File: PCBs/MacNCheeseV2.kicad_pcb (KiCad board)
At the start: 2 copper layers, 102.4 x 81 mm, 33 parts, among them SW1 SW_Push, SW10 SW_Push, SW11 SW_Push, SW12 SW_Push, SW13 SW_Push, SW14 SW_Push, SW15 SW_Push, SW16 SW_Push, SW2 SW_Push, SW3 SW_Push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

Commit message: PCBs V2.1
Added Designs
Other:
- board text added: "7763"
- board text added: "Emily is Awesome!!"
- board text added: "What a Super Idea"
- board text removed: "Why?"
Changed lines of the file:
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@@
 		)
 		(fp_text user "K"
-			(at 0 -2.1 90)
+			(at 0 0 90)
 			(layer "F.SilkS")
 			(effects
@@
 		)
 		(fp_text user "K"
-			(at 0 -2.1 90)
+			(at 0 0 90)
 			(layer "F.Fab")
 			(effects
@@
 		)
 	)
+	(gr_text "7763"
+		(at 136.75 32.75 0)
+		(layer "F.SilkS")
+		(effects
+			(font
+				(size 1 1)
+				(thickness 0.1)
+			)
+			(justify left bottom)
+		)
+	)
 	(gr_text "XIAO HERE"
 		(at 144.5 50.25 0)
@@
 		)
 	)
+	(gr_text "Emily is Awesome!!"
+		(at 62.75 65.25 270)
+		(layer "F.SilkS")
+		(effects
+			(font
+				(size 1 1)
+				(thickness 0.1)
+			)
+			(justify left bottom)
+		)
+	)
 	(gr_text "YOTC"
 		(at 64 111.5 0)
@@
 		)
 	)
-	(gr_text "Why?"
+	(gr_text "What a Super Idea"
 		(at 64 32.75 0)
 		(layer "F.SilkS")

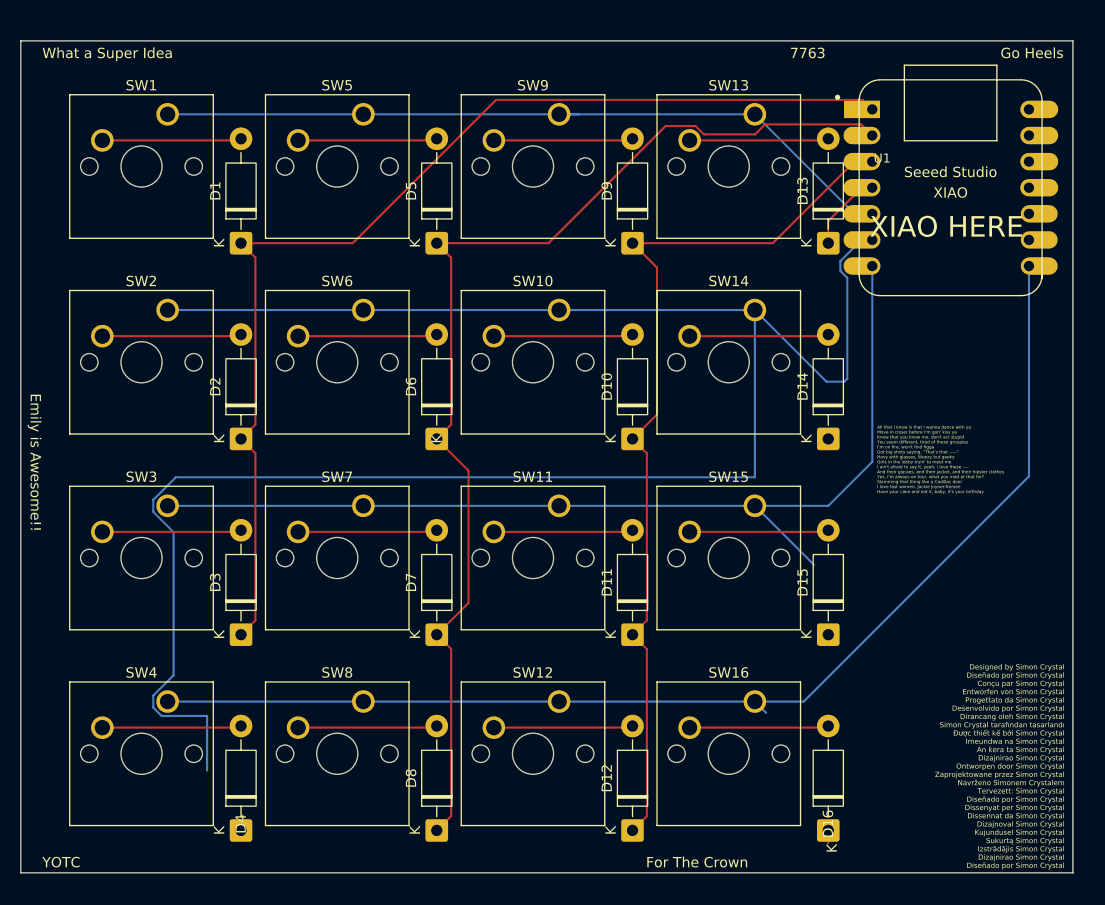
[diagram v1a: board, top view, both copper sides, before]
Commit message: PCB V2.2
Slight design changes to make in <100mm
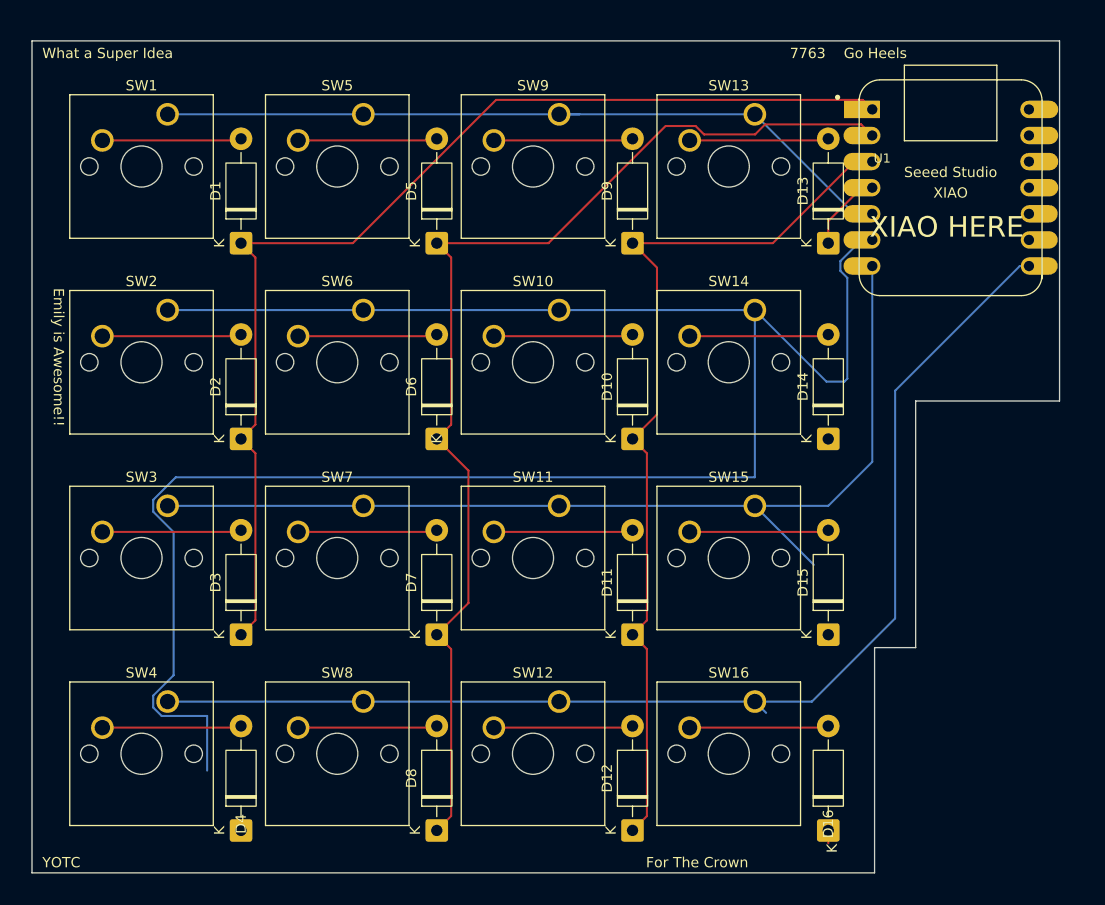
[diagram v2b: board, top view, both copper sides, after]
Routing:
- net /COL3: track 114.9 -> 115.9 mm
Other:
- board size 102.4 x 81 mm -> 100 x 81 mm
- board text removed: "All that I know is that I wanna dance with ya Move in closer before I'm gon' kiss ya Know that you know me, don't act stupid You seem different, tired of these groupies I'm on fire, won't find figga Got big shots saying, {dblquote}That's that -----{dblquote} Hovy with glasses, Weezy but geeky Girls in the lobby tryin' to meet me I ain't afraid to say it, yeah, I love these ---- And their glasses,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"
- board text removed: "Designed by Simon Crystal Diseñado por Simon Crystal Conçu par Simon Crystal Entworfen von Simon Crystal Progettato da Simon Crystal Desenvolvido por Simon Crystal Dirancang oleh Simon Crystal Simon Crystal tarafından tasarlandı Được thiết kế bởi Simon Crystal Imeundwa na Simon Crystal An ƙera ta Simon Crystal Dizajnirao Simon Crystal Ontworpen door Simon Crystal Zaprojektowane przez Simon Crysta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"
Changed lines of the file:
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@@
 			(outputformat 1)
 			(mirror no)
-			(drillshape 1)
+			(drillshape 0)
 			(scaleselection 1)
 			(outputdirectory "")
@@
 		)
 	)
-	(gr_rect
-		(start 61.9125 30.95625)
-		(end 164.30625 111.91875)
+	(gr_line
+		(start 63 30.95625)
+		(end 63 111.91875)
+		(stroke
+			(width 0.05)
+			(type default)
+		)
+		(layer "Edge.Cuts")
+	)
+	(gr_line
+		(start 63 111.91875)
+		(end 145 111.91875)
+		(stroke
+			(width 0.05)
+			(type default)
+		)
+		(layer "Edge.Cuts")
+	)
+	(gr_line
+		(start 163 30.95625)
+		(end 163 66)
+		(stroke
+			(width 0.05)
+			(type default)
+		)
+		(layer "Edge.Cuts")
+	)
+	(gr_line
+		(start 145 111.91875)
+		(end 145 90)
+		(stroke
+			(width 0.05)
+			(type default)
+		)
+		(layer "Edge.Cuts")
+	)
+	(gr_line
+		(start 163 30.95625)
+		(end 63 30.95625)
+		(stroke
+			(width 0.05)
+			(type default)
+		)
+		(layer "Edge.Cuts")
+	)
+	(gr_line
+		(start 149 66)
+		(end 149 90)
+		(stroke
+			(width 0.05)
+			(type default)
+		)
+		(layer "Edge.Cuts")
+	)
+	(gr_line
+		(start 163 66)
+		(end 149 66)
+		(stroke
+			(width 0.05)
+			(type default)
+		)
+		(layer "Edge.Cuts")
+	)
+	(gr_line
+		(start 149 90)
+		(end 145 90)
 		(stroke
 			(width 0.05)
 			(type default)
 		)
-		(fill no)
 		(layer "Edge.Cuts")
 	)
 	(image
-		(at 152.400001 61.9125)
+		(at 152.000001 61.000001)
 		(layer "F.SilkS")
 		(scale 0.079506)
@@
 	)
 	(gr_text "Emily is Awesome!!"
-		(at 62.75 65.25 270)
+		(at 65 55 270)
 		(layer "F.SilkS")
 		(effects
@@
 	)
 	(gr_text "Go Heels"
-		(at 157.25 32.75 0)
+		(at 142 32.75 0)
 		(layer "F.SilkS")
 		(effects
@@
 		)
 	)
-	(gr_text "Designed by Simon Crystal\nDiseñado por Simon Crystal\nConçu par Simon Crystal\nEntworfen von Simon Crystal\nProgettato da Simon Crystal\nDesenvolvido por Simon Crystal\nDirancang oleh Simon Crystal\nSimon Crystal tarafından tasarlandı\nĐược thiết kế bởi Simon Crystal\nImeundwa na Simon Crystal\nAn ƙera ta Simon Crystal\nDizajnirao Simon Crystal\nOntworpen door Simon Crystal\nZaprojektowane przez Simon Crystal\nNavrženo Simonem Crystalem\nTervezett: Simon Crystal\nDiseñado por Simon Crystal\nDissenyat per Simon Crystal\nDissennat da Simon Crystal\nDizajnoval Simon Crystal\nKujundusel Simon Crystal\nSukurtą Simon Crystal\nIzstrādājis Simon Crystal\nDizajnirao Simon Crystal\nDiseñado por Simon Crystal"
-		(at 163.5 111.5 0)
-		(layer "F.SilkS")
-		(effects
-			(font
-				(size 0.5 0.5)
-				(thickness 0.1)
-			)
-			(justify right bottom)
-		)
-	)
-	(gr_text "All that I know is that I wanna dance with ya\nMove in closer before I'm gon' kiss ya\nKnow that you know me, don't act stupid\nYou seem different, tired of these groupies\nI'm on fire, won't find figga\nGot big shots saying, {dblquote}That's that -----{dblquote}\nHovy with glasses, Weezy but geeky\nGirls in the lobby tryin' to meet me\nI ain't afraid to say it, yeah, I love these ----\nAnd their glasses, and their jacket, and their hipster clothes\nYes, I'm always on tour, what you mad at that for?\nSlamming that thing like a Cadillac door\nI love fast women, Jackie Joyner-Kersee\nHave your cake and eat it, baby, it's your birthday"
-		(at 145.25 75 0)
-		(layer "F.SilkS")
-		(effects
-			(font
-				(size 0.3 0.3)
-				(thickness 0.075)
-			)
-			(justify left bottom)
-		)
-	)
 	(gr_text "What a Super Idea"
 		(at 64 32.75 0)
@@
 	)
 	(segment
-		(start 160.025 52.86375)
-		(end 160.025 73.3375)
+		(start 159.13625 52.86375)
+		(end 160.025 52.86375)
 		(width 0.2)
 		(layer "B.Cu")
@@
 	)
 	(segment
-		(start 160.025 73.3375)
-		(end 138.1125 95.25)
+		(start 147 65)
+		(end 159.13625 52.86375)
+		(width 0.2)
+		(layer "B.Cu")
+		(net 24)
+	)
+	(segment
+		(start 138.900058 95.25)
+		(end 147 87.150058)
 		(width 0.2)
 		(layer "B.Cu")
@@
 	)
 	(segment
+		(start 133.35 95.25)
+		(end 138.900058 95.25)
+		(width 0.2)
+		(layer "B.Cu")
+		(net 24)
+	)
+	(segment
+		(start 147 87.150058)
+		(end 147 65)
+		(width 0.2)
+		(layer "B.Cu")
+		(net 24)
+	)
+	(segment
 		(start 95.25 95.25)
 		(end 114.3 95.25)
@@
 		(width 0.2)
 		(layer "B.Cu")
-		(net 24)
-	)
-	(segment
-		(start 138.1125 95.25)
-		(end 133.35 95.25)
-		(width 0.2)
-		(layer "B.Cu")

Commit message: Add files via upload
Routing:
- net /COL1: track 193.3 -> 71.4 mm
- net /ROW3: track 9.04 -> 70.2 mm
- net /ROW2: track 88.1 -> 115.4 mm
- net /ROW0: track 108.0 -> 128.4 mm
- net /COL2: track 97.5 -> 85.2 mm
- net /COL3: track 115.9 -> 110.6 mm
- net /COL0: track 74.6 -> 72.6 mm
- net /ROW1: track 110.3 -> 111.0 mm
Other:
- board size 100 x 81 mm -> 103 x 84 mm
